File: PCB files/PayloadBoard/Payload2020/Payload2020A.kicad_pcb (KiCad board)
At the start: 2 copper layers, 31.8 x 152.4 mm, 28 parts, among them J1 BATTERY, J2 BridgeConn, J3 LoadCell, Q1 Q_NMOS_GSD, Q2 Q_NMOS_GSD, SW1 SW_SPST, U1 Teensy3.6, U2 ArduCam, U3 HX711_Breakout, U4 AP7370-50W5-7, U5 TPS613222ADBVR

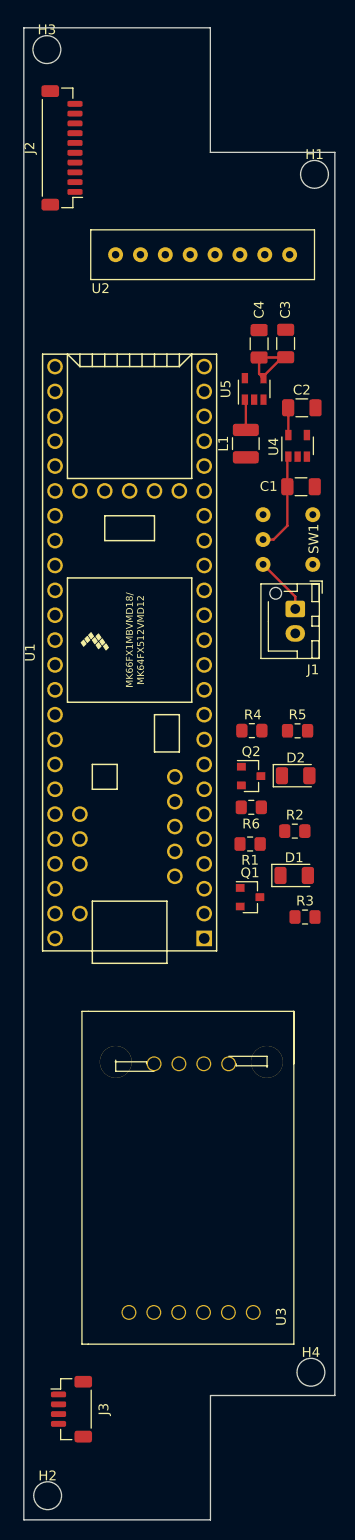
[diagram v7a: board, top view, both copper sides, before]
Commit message: Redrawn edge cuts for board B Redrawn GND planes Changed bridge connector to molex picoblade
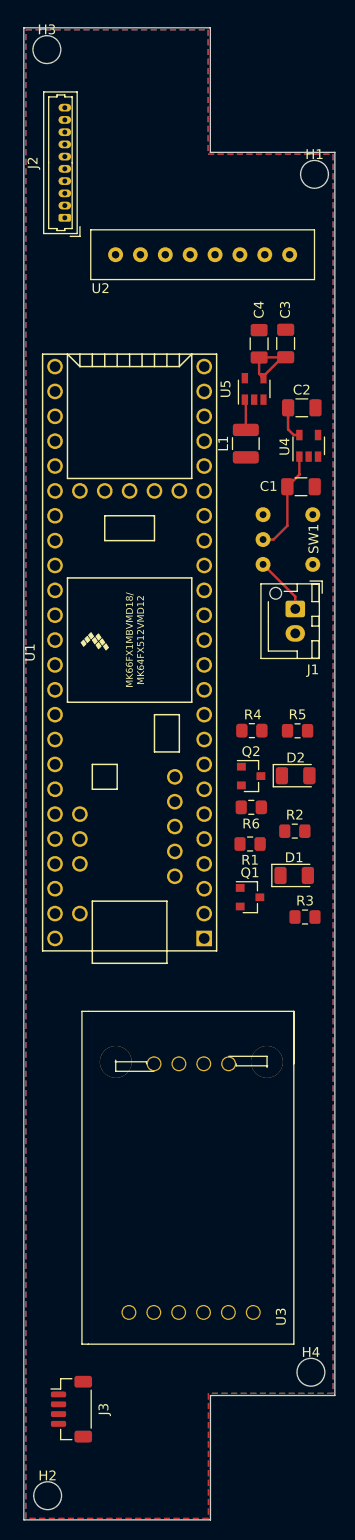
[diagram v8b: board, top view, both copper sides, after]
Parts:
- J2: footprint Connector_JST:JST_SH_BM10B-SRSS-TB_1x10-1MP_P1.00mm_Vertical -> Connector_Molex:Molex_PicoBlade_53047-1010_1x10_P1.25mm_Vertical
- moved J2 7.15 mm to (124.7, 39.9)
- moved U4 1.14 mm to (149.6, 63.2)
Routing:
- net +3.3VA: track 2.79 -> 3.60 mm
- added copper zone on B.Cu, net GNDREF
- added copper zone on F.Cu, net GNDREF
